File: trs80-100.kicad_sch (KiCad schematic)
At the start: 253 parts, among them CN2 A-7224, CN3 TCS-4480, CN4 TCS-4490, CN6 RS232C, J1 Adapter Jack CN9, K1 Key_Board, M15 40H244, M21 40H244, M23 40H244, M27 4011, M28 4013, M29 TL064, M30 TL064, M33 40H157, M34 4584, M35 4584, SW3 SLB-22BP-03, SW4 Reset Switch, SW5 SSP32201, T10 2SC2603, T11 2SC2603, T13 2SC2603, T14 2SC2603(E), T15 2SC2603(E), T16 2SC2603(E), T17 2SC2603(E), T18 2SC2603, T19 2SA1115, T2 2SC2603, T20 2SC2603, T21 2SC2603(E), T22 2SC2603(E), T25 2SC2603, T27 2SC2603, T28 2SA1115, T3 2SC2603, T5 2SC2603, T6 2SC2603, T9 2SC2603

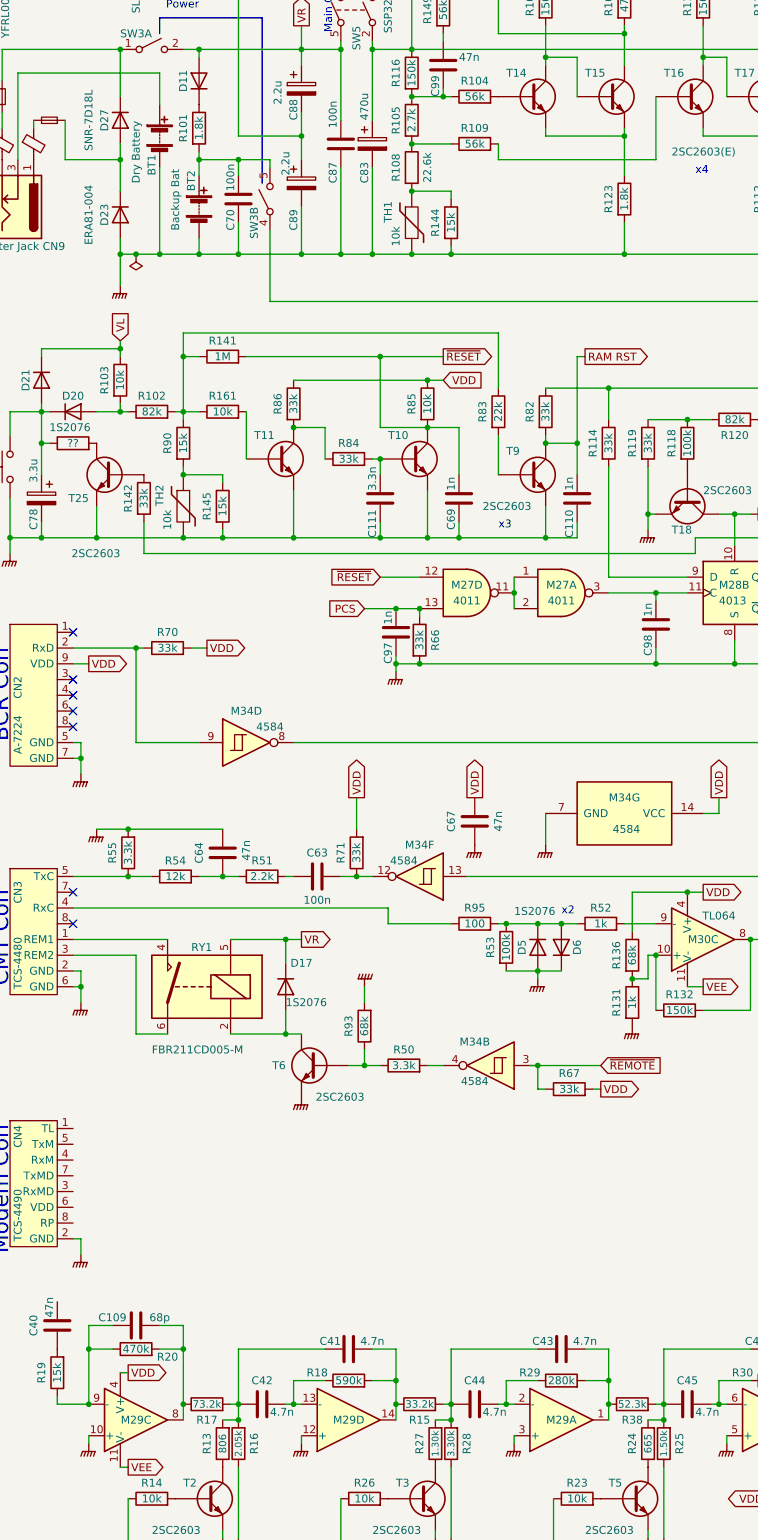
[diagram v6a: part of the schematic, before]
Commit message: Add surge protector symbol
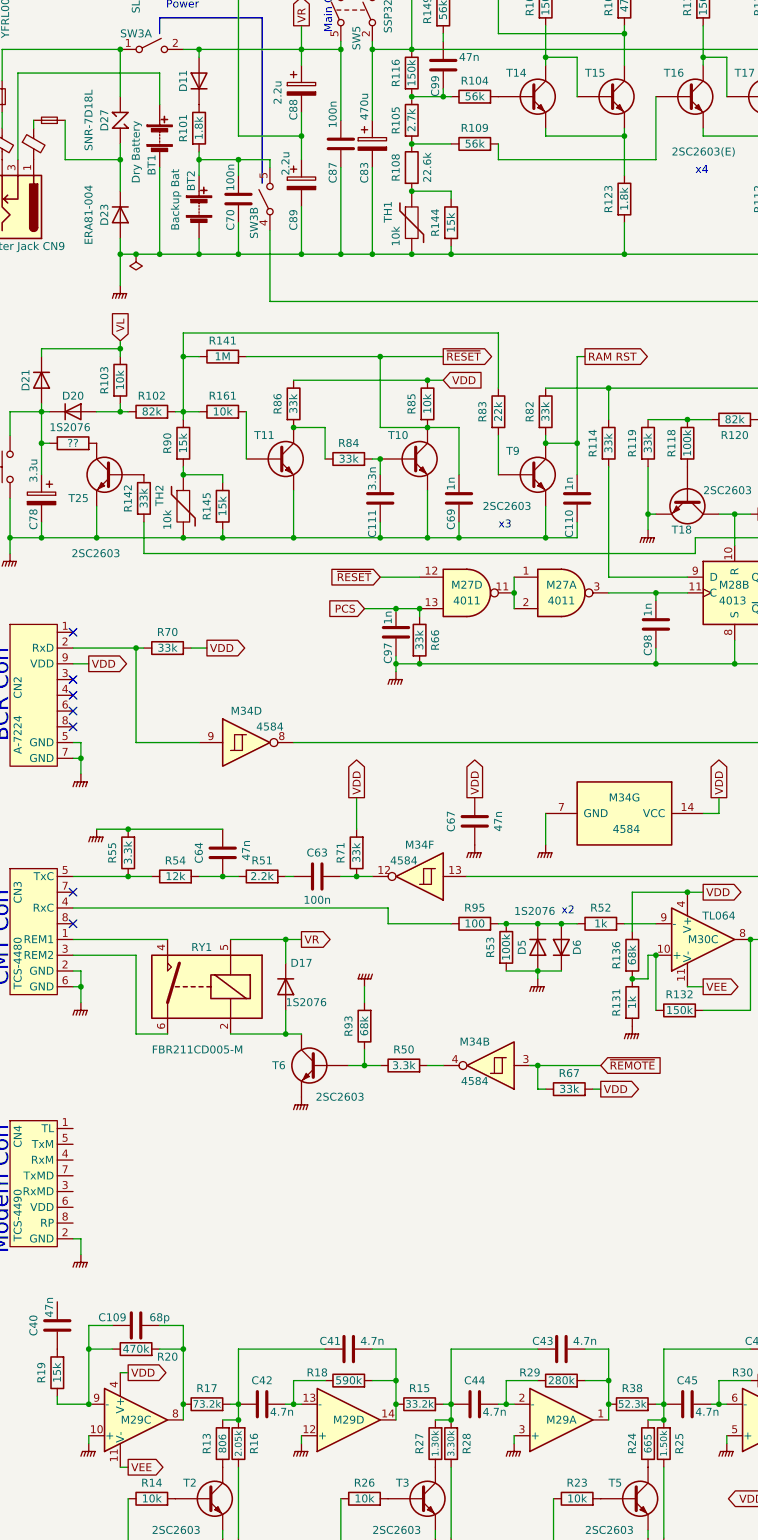
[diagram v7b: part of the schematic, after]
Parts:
- D27: symbol Device:D -> trs80-100:surge-absorber
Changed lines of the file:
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@@
     (pin "1")
   )
-  (symbol (lib_id "Device:D") (at 39.37 46.99 270) (unit 1)
+  (symbol (lib_id "trs80-100:surge-absorber") (at 39.37 46.99 270) (unit 1)
     (in_bom yes) (on_board yes)
     (property "Reference" "D27" (id 0) (at 36.83 46.99 0))
     (property "Value" "SNR-7D18L" (id 1) (at 34.29 46.99 0))
-    (property "Footprint" "" (id 2) (at 39.37 46.99 0)
-      (effects (font (size 1.27 1.27)) hide)
-    )
-    (property "Datasheet" "~" (id 3) (at 39.37 46.99 0)
+    (property "Footprint" "" (id 2) (at 34.925 48.26 0)
+      (effects (font (size 1.27 1.27)) hide)
+    )
+    (property "Datasheet" "~" (id 3) (at 39.37 48.26 0)
       (effects (font (size 1.27 1.27)) hide)
     )
@@
   (symbol (lib_id "Device:R") (at 121.92 254 90) (unit 1)
     (in_bom yes) (on_board yes)
-    (property "Reference" "R38" (id 0) (at 121.92 256.54 90))
+    (property "Reference" "R38" (id 0) (at 121.92 251.46 90))
     (property "Value" "52.3k" (id 1) (at 121.92 254 90)
       (effects (font (size 1.2 1.2)))
@@
   (symbol (lib_id "Device:R") (at 53.34 254 90) (unit 1)
     (in_bom yes) (on_board yes)
-    (property "Reference" "R17" (id 0) (at 53.34 256.54 90))
+    (property "Reference" "R17" (id 0) (at 53.34 251.46 90))
     (property "Value" "73.2k" (id 1) (at 53.34 254 90)
       (effects (font (size 1.2 1.2)))
@@
   (symbol (lib_id "Device:R") (at 87.63 254 90) (unit 1)
     (in_bom yes) (on_board yes)
-    (property "Reference" "R15" (id 0) (at 87.63 256.54 90))
+    (property "Reference" "R15" (id 0) (at 87.63 251.46 90))
     (property "Value" "33.2k" (id 1) (at 87.63 254 90)
       (effects (font (size 1.2 1.2)))

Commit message: Add ROM and RAM symbols.
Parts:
- added C11, C9: 100n, symbol Device:C_Small
- added C5, C6, C7, C8: 1u, symbol Device:C_Polarized_Small
- added M11, M12: ROM32k, symbol trs80-100:ROM32k
- added M6: OPTION RAM #3, symbol trs80-100:RAM_4x2kiB
- added M7: OPTION RAM #2, symbol trs80-100:RAM_4x2kiB
- added M8: OPTION RAM #1, symbol trs80-100:RAM_4x2kiB
- added M9: STANDARD RAM, symbol trs80-100:RAM_4x2kiB
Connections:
- net AD0: now also M11.11 (AD0), M12.11 (AD0), M6.9 (AD0), M7.9 (AD0), M8.9 (AD0), M9.9 (AD0)
- net AD1: now also M11.12 (AD1), M12.12 (AD1), M6.10 (AD1), M7.10 (AD1), M8.10 (AD1), M9.10 (AD1)
- net AD2: now also M11.13 (AD2), M12.13 (AD2), M6.11 (AD2), M7.11 (AD2), M8.11 (AD2), M9.11 (AD2)
- net AD3: now also M11.15 (AD3), M12.15 (AD3), M6.17 (AD3), M7.17 (AD3), M8.17 (AD3), M9.17 (AD3)
- net AD4: now also M11.16 (AD4), M12.16 (AD4), M6.18 (AD4), M7.18 (AD4), M8.18 (AD4), M9.18 (AD4)
- net AD5: now also M11.17 (AD5), M12.17 (AD5), M6.19 (AD5), M7.19 (AD5), M8.19 (AD5), M9.19 (AD5)
- net AD6: now also M11.18 (AD6), M12.18 (AD6), M6.20 (AD6), M7.20 (AD6), M8.20 (AD6), M9.20 (AD6)
- net AD7: now also M11.19 (AD7), M12.19 (AD7), M6.21 (AD7), M7.21 (AD7), M8.21 (AD7), M9.21 (AD7)
- net GNDPWR: now also C11.2, C5.2, C6.2, C7.2, C8.2, C9.2, M11.14 (GND), M12.14 (GND), M6.12 (GND), M6.16 (GND), M7.12 (GND), M7.16 (GND), M8.12 (GND), M8.16 (GND), M9.12 (GND), M9.16 (GND)
- net RAM RST: now also M6.22 (~{OE}), M7.22 (~{OE}), M8.22 (~{OE}), M9.22 (~{OE})
- net VB: now also C5.1, C6.1, C7.1, C8.1, M6.28 (VDD), M7.28 (VDD), M8.28 (VDD), M9.28 (VDD)
- net VDD: now also C11.1, C9.1, M11.1 (VDD), M12.1 (VDD)
- new net A0: M11.10 (A0), M12.10 (A0), M6.8 (A0), M7.8 (A0), M8.8 (A0), M9.8 (A0)
- new net A1: M11.9 (A1), M12.9 (A1), M6.7 (A1), M7.7 (A1), M8.7 (A1), M9.7 (A1)
- new net A10: M11.2 (A10), M12.2 (A10), M6.23 (A10), M7.23 (A10), M8.23 (A10), M9.23 (A10)
- new net A11: M11.20 (A11), M12.20 (A11)
- new net A12: M11.24 (A12), M12.24 (A12)
- new net A13: M11.22 (A13), M12.22 (A13)
- new net A14: M11.28 (A14), M12.28 (A14)
- new net A2: M11.8 (A2), M12.8 (A2), M6.6 (A2), M7.6 (A2), M8.6 (A2), M9.6 (A2)
- new net A3: M11.7 (A3), M12.7 (A3), M6.5 (A3), M7.5 (A3), M8.5 (A3), M9.5 (A3)
- new net A4: M11.6 (A4), M12.6 (A4), M6.4 (A4), M7.4 (A4), M8.4 (A4), M9.4 (A4)
- new net A5: M11.5 (A5), M12.5 (A5), M6.3 (A5), M7.3 (A5), M8.3 (A5), M9.3 (A5)
- new net A6: M11.4 (A6), M12.4 (A6), M6.2 (A6), M7.2 (A6), M8.2 (A6), M9.2 (A6)
- new net A7: M11.3 (A7), M12.3 (A7), M6.1 (A7), M7.1 (A7), M8.1 (A7), M9.1 (A7)
- new net A8: M11.26 (A8), M12.26 (A8), M6.27 (A8), M7.27 (A8), M8.27 (A8), M9.27 (A8)
- new net A9: M11.25 (A9), M12.25 (A9), M6.26 (A9), M7.26 (A9), M8.26 (A9), M9.26 (A9)
- new net ~{WR}*: M6.25 (~{WR}), M7.25 (~{WR}), M8.25 (~{WR}), M9.25 (~{WR})
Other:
- note added: "Option ROM"
- note added: "Standard ROM"
- moved on the sheet: C20, C21, C22, C23, C24, C25, C26, C27, M15, MR4A
